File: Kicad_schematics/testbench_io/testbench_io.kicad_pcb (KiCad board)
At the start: 2 copper layers, 67 parts, among them J1 Conn_01x02, J102 Conn_01x02, J103 Conn_01x02, J104 DB37_Female_MountingHoles, J301 Conn_01x04, Q101 BUK9M42-60EX, Q201 2N3904, Q301 BUK9M42-60EX, Q302 BUK9M42-60EX, Q303 BUK9M42-60EX, Q304 BUK9M42-60EX, SW1 SW_DIP_x01, SW101 SW_SPST, SW102 SW_SPST, SW103 SW_Push, SW104 SW_Push, SW105 SW_Push, SW106 SW_SPST, SW107 SW_SPST, SW108 SW_SPST, SW109 SW_DIP_x08, SW110 SW_Push, SW111 SW_SPST, SW112 SW_SPST, SW113 SW_SPST, SW114 SW_SPST, SW115 SW_Push, U101 NUCLEO64-F476RG, U102 CJMCU_MCP2551, U201 PCF8574AN

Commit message: Pcb-layout is on the way
Signed-off-by: Mojitas <47667093+Mojitas@users.noreply.github.com>
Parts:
- D201, J1, J102, J103, J104, J301, JP201, JP202, JP203, Q201, R107, R201, R202, R203, R204, R205, R206, R301, R302, R303, R304, RV201, SW1, U102, U201: moved to B.Cu
- DS201: value HY1602E -> WC1602A
- Q101, Q301, Q302, Q303, Q304: value BUK9M42-60EX -> IPD50R380CE; moved to B.Cu
- U101: footprint Solar_team:MODULE_NUCLEO-F446RE -> Solar_team:MODULE_NUCLEO-F476RG; moved to B.Cu
- moved RV101 293.2 mm to (73.5, 179.0), turned to 90 degrees
- moved Q201 289.1 mm to (81.3, 103.6), turned to 90 degrees
- moved U101 284.5 mm to (247.7, 141.0)
- moved SW111 275.8 mm to (63.6, 146.3), turned to 90 degrees
- moved Q301 273.8 mm to (147.8, 190.2), turned to 90 degrees
- moved D201 272.2 mm to (57.1, 116.8), turned to 180 degrees
- moved R205 270.8 mm to (61.7, 117.2)
- moved R301 270.7 mm to (147.8, 198.7)
- moved JP201 269.8 mm to (82.8, 115.8), turned to 270 degrees
- moved R201 267.9 mm to (46.2, 115.5), turned to 90 degrees
- moved C201 266.4 mm to (102.7, 118.6)
- moved JP202 266.0 mm to (88.4, 116.0), turned to 270 degrees
- moved Q303 264.8 mm to (170.6, 190.2), turned to 90 degrees
- moved RV103 263.5 mm to (100.0, 179.0), turned to 90 degrees
- moved R302 263.0 mm to (158.6, 198.7)
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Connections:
- DS201 pad 1: /LCD_I2C/LED_(-) -> GND
- DS201 pad 11: Net-(DS201-Pad11) -> /LCD_I2C/DB4
- DS201 pad 12: Net-(DS201-Pad12) -> /LCD_I2C/DB5
- DS201 pad 13: /LCD_I2C/DB4 -> /LCD_I2C/DB6
- DS201 pad 14: /LCD_I2C/DB5 -> /LCD_I2C/DB7
- DS201 pad 15: /LCD_I2C/DB6 -> /LCD_I2C/LED_(+)
- DS201 pad 16: /LCD_I2C/DB7 -> /LCD_I2C/LED_(-)
- DS201 pad 2: /LCD_I2C/LED_(+) -> MCU_5V
- DS201 pad 3: GND -> /LCD_I2C/pot_brightness
- DS201 pad 4: MCU_5V -> /LCD_I2C/RS
- DS201 pad 5: /LCD_I2C/pot_brightness -> /LCD_I2C/RW
- DS201 pad 6: /LCD_I2C/RS -> /LCD_I2C/E
- DS201 pad 7: /LCD_I2C/RW -> Net-(DS201-Pad7)
- DS201 pad 8: /LCD_I2C/E -> Net-(DS201-Pad8)
- Q101 pad 1: GND -> /Fan_pwm
- Q101 pad 2: GND -> VDD_MCU
- Q301 pad 1: GND -> /Solar_lights/Brake_acti
- Q301 pad 2: GND -> /Solar_lights/Brake_lights_pwr
- Q302 pad 1: GND -> /Solar_lights/Left_acti
- Q302 pad 2: GND -> /Solar_lights/Left_indicator_pwr
- Q303 pad 1: GND -> /Solar_lights/Right_acti
- Q303 pad 2: GND -> /Solar_lights/Right_indicator_pwr
- Q304 pad 1: GND -> /Solar_lights/Front_acti
- Q304 pad 2: GND -> /Solar_lights/Front_lights_pwr
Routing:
- net GND: track 0.00 -> 134.0 mm
- net MCU_5V: track 0.00 -> 127.3 mm
- net /Solar_lights/Front_lights_pwr: track 0.00 -> 81.1 mm
- net /Solar_lights/Right_indicator_pwr: track 0.00 -> 65.2 mm
- net /Solar_lights/Left_indicator_pwr: track 0.00 -> 49.8 mm
- net /Solar_lights/Brake_lights_pwr: track 0.00 -> 32.9 mm
- net /TRM_15: track 0.00 -> 32.5 mm
- net /LCD_I2C/RS: track 0.00 -> 32.2 mm
- net Net-(J1-Pad1): track 0.00 -> 32.1 mm
- net Net-(JP203-Pad1): track 0.00 -> 29.3 mm
- net /LCD_I2C/RW: track 0.00 -> 27.1 mm
- net Net-(J1-Pad2): track 0.00 -> 26.1 mm
- net Net-(JP202-Pad1): track 0.00 -> 24.4 mm
- net /LCD_I2C/E: track 0.00 -> 21.7 mm
- net Net-(JP201-Pad1): track 0.00 -> 19.4 mm
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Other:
- board text added: "Battery_pot"

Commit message: Routing done and power planes added
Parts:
- removed Q101: IPD50R380CE, Package_TO_SOT_SMD:TO-252-2
- removed R107: R_Small, Resistor_SMD:R_0603_1608Metric
- removed the SW102 at (200.5, 146.3)
- removed the SW108 at (171.2, 172.4)
- added H101: MountingHole_Pad, MountingHole:MountingHole_3.2mm_M3_Pad_Via, F.Cu at (110.7, 87.9)
- added H102: MountingHole_Pad, MountingHole:MountingHole_3.2mm_M3_Pad_Via, F.Cu at (24.4, 87.9)
- added H103: MountingHole_Pad, MountingHole:MountingHole_3.2mm_M3_Pad_Via, F.Cu at (24.4, 207.9)
- added H104: MountingHole_Pad, MountingHole:MountingHole_3.2mm_M3_Pad_Via, F.Cu at (197.0, 207.9)
- added H105: MountingHole_Pad, MountingHole:MountingHole_3.2mm_M3_Pad_Via, F.Cu at (197.0, 87.9)
- added Q305: IPD50R380CE, Package_TO_SOT_SMD:TO-252-2, B.Cu at (62.2, 188.8)
- added Q306: IPD50R380CE, Package_TO_SOT_SMD:TO-252-2, B.Cu at (51.6, 188.8)
- added R305: R_Small, Resistor_SMD:R_0603_1608Metric, B.Cu at (62.6, 181.2)
- added R306: R_Small, Resistor_SMD:R_0603_1608Metric, B.Cu at (51.5, 181.2)
- added SW109: SW_SPST, Solar_team:RND-Slide-Switch, F.Cu at (148.0, 159.2)
- C201: footprint Package_TO_SOT_SMD:TO-252-2 -> Capacitor_SMD:C_0805_2012Metric
- J104: footprint Connector_Dsub:DSUB-37_Female_EdgeMount_P2.77mm -> Connector_Dsub:DSUB-37_Female_Horizontal_P2.77x2.84mm_EdgePinOffset7.70mm_Housed_MountingHolesOffset9.12mm
- J301: value Conn_01x04 -> Conn_01x12; footprint Connector_JST:JST_XH_S4B-XH-A-1_1x04_P2.50mm_Horizontal -> Connector_JST:JST_XH_S12B-XH-A-1_1x12_P2.50mm_Horizontal
- JP101, R101, R102, R103, R104, R105, R106, R108, R207: moved to B.Cu
- SW101, SW106, SW107, SW111, SW112, SW113: footprint Solar_team:MTS-102-A2 -> Solar_team:RND-Slide-Switch
- SW108: renamed from SW109; moved to B.Cu
- SW114: value SW_SPST -> SW_DPDT_x2; footprint Solar_team:MTS-102-A2 -> Solar_team:RND-Slide-Switch
- U102: moved to F.Cu
- moved SW105 164.0 mm to (31.8, 135.8)
- moved RV102 143.9 mm to (62.5, 165.2)
- moved SW108 140.5 mm to (133.1, 180.8)
- moved J104 115.4 mm to (133.1, 195.1), turned to 180 degrees
- moved R304 112.0 mm to (73.1, 181.2), turned to 180 degrees
- moved Q304 110.9 mm to (72.7, 188.8), turned to 270 degrees
- moved JP101 104.6 mm to (169.7, 181.7)
- moved U102 103.3 mm to (170.9, 182.6), turned to 0 degrees
- moved SW111 102.9 mm to (166.1, 138.3), turned to 0 degrees
- moved D106 100.9 mm to (185.0, 177.5)
- moved R104 100.9 mm to (165.1, 181.7), turned to 0 degrees
- moved U101 97.5 mm to (152.8, 118.4), turned to 270 degrees
- moved R108 93.2 mm to (181.3, 179.3), turned to 270 degrees
- moved R303 88.7 mm to (83.5, 181.6), turned to 180 degrees
- moved Q303 87.2 mm to (83.3, 188.8), turned to 270 degrees
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- renumbered J103 to J101, J1 to J102, J102 to J103, SW103 to SW102, SW104 to SW103, SW105 to SW104, SW115 to SW105, SW1 to SW201
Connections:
- net Net-(U101-Pad41) renamed /CRX
- J101 pad 1: Net-(J103-Pad1) -> Net-(J101-Pad1)
- J101 pad 2: Net-(J103-Pad2) -> Net-(J101-Pad2)
- J301 pad 1: /Solar_lights/Brake_lights_pwr -> VDD_MCU
- J301 pad 2: /Solar_lights/Left_indicator_pwr -> /Solar_lights/Brake_lights_VSS
- J301 pad 3: /Solar_lights/Right_indicator_pwr -> VDD_MCU
- J301 pad 4: /Solar_lights/Front_lights_pwr -> /Solar_lights/Left_indicator_VSS
- Q301 pad 1: /Solar_lights/Brake_acti -> /Brake_acti
- Q301 pad 2: /Solar_lights/Brake_lights_pwr -> /Solar_lights/Brake_lights_VSS
- Q302 pad 1: /Solar_lights/Left_acti -> /Left_acti
- Q302 pad 2: /Solar_lights/Left_indicator_pwr -> /Solar_lights/Left_indicator_VSS
- Q303 pad 1: /Solar_lights/Right_acti -> /Right_acti
- Q303 pad 2: /Solar_lights/Right_indicator_pwr -> /Solar_lights/Right_indicator_VSS
- Q304 pad 1: /Solar_lights/Front_acti -> /Front_acti
- Q304 pad 2: /Solar_lights/Front_lights_pwr -> /Solar_lights/Front_lights_VSS
- R205 pad 2: /LCD_I2C/SDA -> /SDA
- R206 pad 2: /LCD_I2C/SCL -> /SCL
- R301 pad 2: /Solar_lights/Brake_acti -> /Brake_acti
- R302 pad 2: /Solar_lights/Left_acti -> /Left_acti
- R303 pad 2: /Solar_lights/Right_acti -> /Right_acti
- R304 pad 2: /Solar_lights/Front_acti -> /Front_acti
- SW108 pad 10: TRM_VDD -> /TRM_25
- SW108 pad 11: /TRM_15 -> /TRM_05
- SW108 pad 12: /TRM_05 -> TRM_GND
- SW108 pad 13: /TRM_25 -> /TRM_22
- SW108 pad 14: /TRM_22 -> TRM_VDD
- SW108 pad 3: /Brake_vol -> MCU_5V
- SW108 pad 4: /F-R_sw -> /Brake_vol
- SW108 pad 5: /P-E_sw -> GND
- SW108 pad 6: /MC_LED -> /P-E_sw
- SW108 pad 7: MCU_5V -> /F-R_sw
- SW108 pad 8: GND -> /MC_LED
- SW108 pad 9: TRM_GND -> /TRM_15
- SW111 pad 1: /DRL_sw -> Net-(J101-Pad2)
- SW111 pad 2: GND -> Net-(J101-Pad1)
- SW112 pad 1: /HL_sw -> /DRL_sw
- SW113 pad 1: GND -> /HL_sw
- SW113 pad 2: /Left_sw -> GND
- SW114 pad 1: GND -> /Left_sw
- SW114 pad 2: /Right_sw -> GND
- U101 pad 13: /Left_LED -> Net-(U101-Pad13)
- U101 pad 15: /Right_LED -> /Right_sw
- U101 pad 17: Net-(U101-Pad17) -> /Left_sw
- U101 pad 21: /Solar_lights/Right_acti -> Net-(U101-Pad21)
- U101 pad 27: /Horn_sw -> Net-(U101-Pad27)
- U101 pad 28: /Battery_pot -> Net-(U101-Pad28)
- U101 pad 29: /Left_sw -> Net-(U101-Pad29)
- U101 pad 30: /Fan_pot -> Net-(U101-Pad30)
- U101 pad 31: /Right_sw -> /Left_LED
- U101 pad 32: /Acc_vol -> /Battery_LED
- U101 pad 34: /Brake_vol -> /DRL_LED
- U101 pad 35: Net-(U101-Pad35) -> /Right_LED
- U101 pad 36: Net-(U101-Pad36) -> /SDA
- U101 pad 37: Net-(U101-Pad37) -> /Brake_LED
- U101 pad 38: Net-(U101-Pad38) -> /SCL
- U101 pad 39: /DRL_LED -> /Select
- U101 pad 40: /Battery_LED -> /Down
- U101 pad 42: /Brake_LED -> /Fan_pwm
- U101 pad 44: Net-(U101-Pad44) -> /Front_acti
- U101 pad 49: Net-(U101-Pad49) -> /Horn_acti
- U101 pad 50: Net-(U101-Pad50) -> /Right_acti
- U101 pad 51: Net-(U101-Pad51) -> /Fan_pot
- U101 pad 52: /MC_sw -> /Left_acti
- U101 pad 53: Net-(U101-Pad53) -> /Battery_pot
- U101 pad 54: Net-(U101-Pad54) -> /Brake_acti
- U101 pad 55: /Fan_pwm -> /Up
- U101 pad 57: /Select -> /Horn_sw
- U101 pad 59: /Up -> Net-(U101-Pad59)
- U101 pad 60: /P-E_sw -> /MC_sw
- U101 pad 61: /Down -> Net-(U101-Pad61)
- U101 pad 62: /F-R_sw -> /Acc_vol
- U101 pad 64: Net-(U101-Pad64) -> /Brake_vol
- U101 pad 65: /Solar_lights/Front_acti -> Net-(U101-Pad65)
- U101 pad 66: /LCD_I2C/SCL -> /P-E_sw
- U101 pad 67: /Solar_lights/Brake_acti -> Net-(U101-Pad67)
- U101 pad 68: /LCD_I2C/SDA -> /F-R_sw
- U101 pad 69: /Solar_lights/Left_acti -> Net-(U101-Pad69)
- U101 pad 71: /MC_LED -> Net-(U101-Pad71)
- U101 pad 72: Net-(U101-Pad72) -> /MC_LED
- U102 pad 3: Net-(U101-Pad43) -> /CTX
- U201 pad 14: /LCD_I2C/SCL -> /SCL
- U201 pad 15: /LCD_I2C/SDA -> /SDA
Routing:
- net GND: track 134.0 -> 868.1 mm, vias 0 -> 1
- net MCU_5V: track 127.3 -> 492.8 mm, vias 0 -> 3
- net VDD_MCU: track 0.00 -> 350.4 mm
- net Net-(J101-Pad2): track 0.00 -> 189.7 mm
- net V_external: track 0.00 -> 189.3 mm
- net Net-(J101-Pad1): track 0.00 -> 181.7 mm
- net /Reset: track 12.5 -> 183.7 mm
- net /DRL_sw: track 0.00 -> 148.6 mm
- net /SDA: track 0.00 -> 141.1 mm
- net /Down: track 12.5 -> 153.4 mm
- net /SCL: track 0.00 -> 138.6 mm
- net /Horn_acti: track 0.00 -> 134.4 mm, vias 0 -> 1
- net /HL_sw: track 0.00 -> 127.3 mm
- net /Up: track 12.5 -> 139.2 mm
- net /Select: track 12.5 -> 135.1 mm
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- added copper zone on B.Cu, net GND
- added copper zone on F.Cu, net MCU_5V
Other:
- board outline added: 182.6 x 130 mm
- board text added: "Acceleration volume"
- board text added: "Battery"
- board text added: "Battery potentiometer"
- board text added: "Brake"
- board text added: "Brake volume"
- board text added: "DRL"
- board text added: "Direction"
- board text added: "Down"
- board text added: "Drive mode"
- board text added: "Eco"
- board text added: "Fan potentiometer"
- board text added: "Forward"
- board text added: "Hazard lights"
- board text added: "Horn"
- board text added: "I2C adress jumpers"
- board text added: "Left"
- board text added: "Left indicator"
- board text added: "MCU reset"
- board text added: "Motor controller"
- board text added: "Motor controller Heat warning"
- board text added: "Off"
- board text added: "On"
- board text added: "Power"
- board text added: "Reverse"
- board text added: "Right"
- board text added: "Right indicator"
- board text added: "Safe State"
- board text added: "Select"
- board text added: "Turn indicator"
- board text added: "Up"
- board text removed: "Battery_pot"

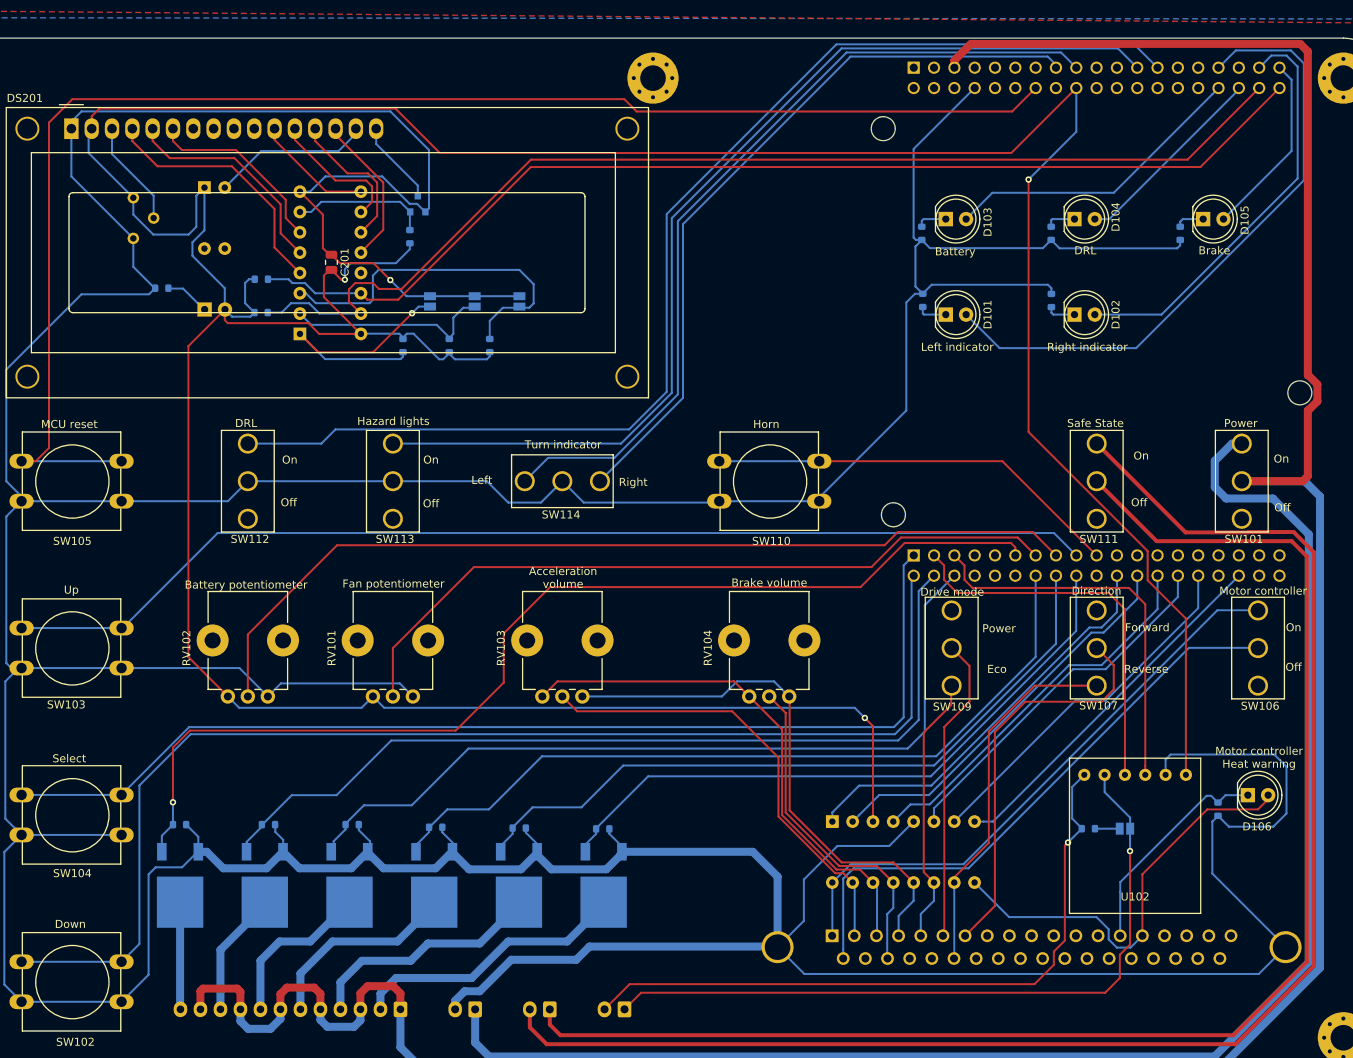
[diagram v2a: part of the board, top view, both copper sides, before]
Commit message: Removed redundant tracks
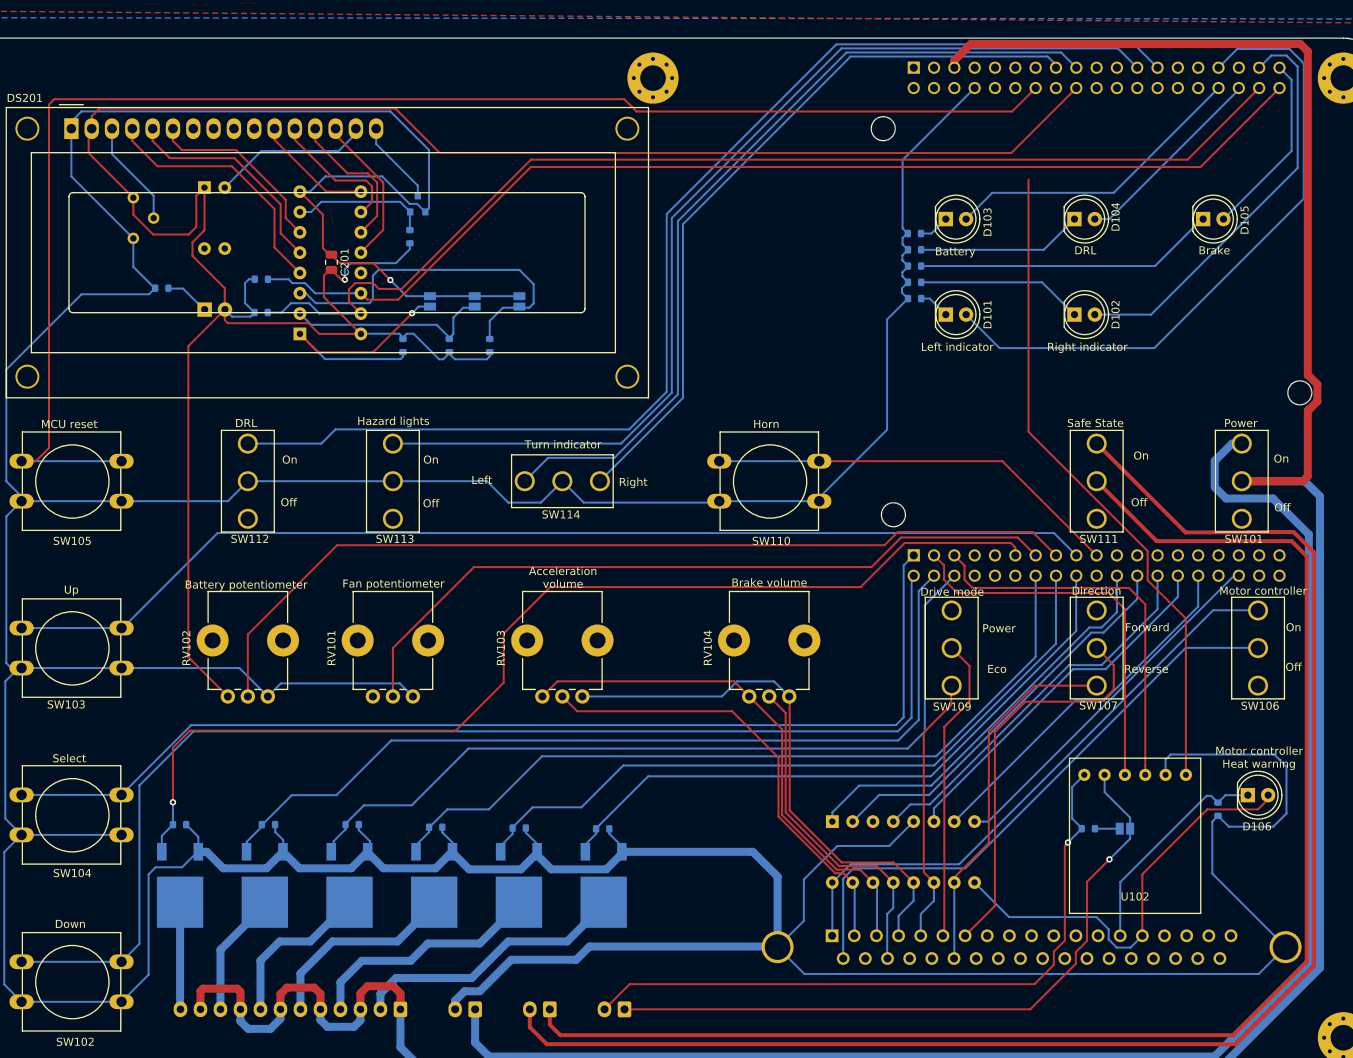
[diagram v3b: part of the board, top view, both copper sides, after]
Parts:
- moved R106 33.5 mm to (143.4, 111.4), turned to 180 degrees
- moved R102 17.2 mm to (143.4, 113.4), turned to 180 degrees
- moved R105 17.2 mm to (143.4, 109.4), turned to 180 degrees
- moved R101 1.04 mm to (143.4, 115.5), turned to 180 degrees
- moved R103 0.92 mm to (143.4, 107.3), turned to 180 degrees
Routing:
- net MCU_5V: track 492.8 -> 383.6 mm, vias 3 -> 1
- net GND: track 868.1 -> 816.5 mm
- net Net-(D105-Pad1): track 3.63 -> 37.7 mm
- net Net-(D102-Pad1): track 3.69 -> 20.8 mm
- net Net-(D104-Pad1): track 3.78 -> 20.8 mm
- net Net-(J102-Pad1): track 90.8 -> 86.5 mm
- net /Left_LED: track 79.5 -> 81.0 mm
- net /Reset: track 183.7 -> 185.0 mm
- net /Right_LED: track 52.4 -> 51.6 mm

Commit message: Added some final text about external connectors
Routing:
- net VDD_MCU: track 350.4 -> 343.8 mm
- net V_external: track 189.3 -> 188.8 mm
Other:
- board text added: "7-12V"
- board text added: "CAN"
- board text added: "Safe state"
- board text added: "Signaling and fan"
